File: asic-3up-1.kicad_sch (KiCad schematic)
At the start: 64 parts, among them J14 Conn_01x01, J15 Conn_01x01, J5 Conn_01x01, J7 Conn_01x01, U48 MCP1824T-1202E/OT, U49 MCP1824T-1202E/OT, U50 MCP1824T-1202E/OT, U51 MCP1824T-0802E, U52 MCP1824T-0802E, U53 MCP1824T-0802E, U54 BM1362AC_MODE1, U55 BM1362AC_MODE0, U56 BM1362AC_MODE1

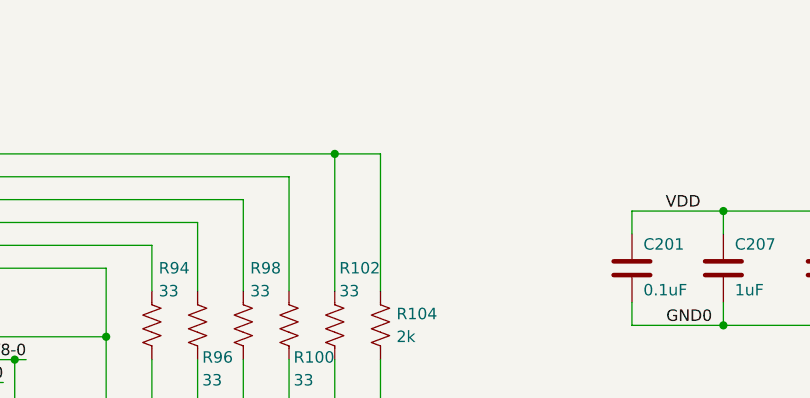
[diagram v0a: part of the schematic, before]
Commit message: added RI pullup resistors for #16. updated BOM. bumped version number to 3
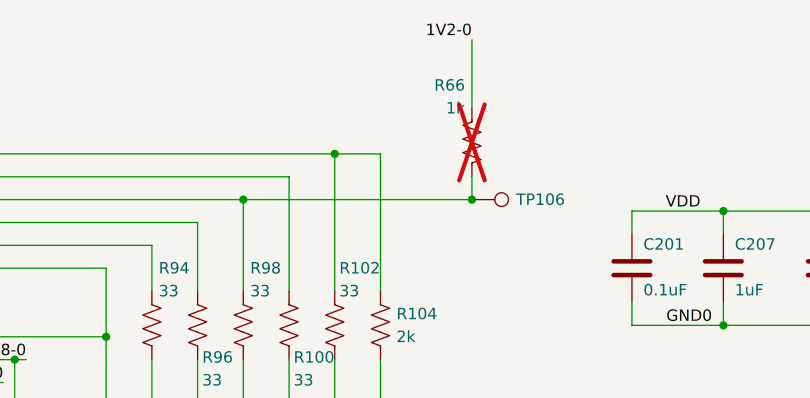
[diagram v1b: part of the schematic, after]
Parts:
- added R66: 1k, Resistor_SMD:R_0402_1005Metric, symbol Device:R_US
- added TP106: TestPoint, TestPoint:TestPoint_Pad_D1.0mm, symbol Connector:TestPoint
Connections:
- net 1V2-0: now also R66.1
- net at R98.1, U54.21 (RI): now also R66.2, TP106.1
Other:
- title: (none) -> emberOne/00
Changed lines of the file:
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@@
 	(paper "A3")
 	(title_block
-		(date "2024-11-25")
-		(rev "2")
+		(title "emberOne/00")
+		(date "2025-02-25")
+		(rev "3")
 	)
 	(text "Reference Voltage Regulators"
@@
 	)
 	(junction
+		(at 328.93 66.04)
+		(diameter 0)
+		(color 0 0 0 0)
+	)
+	(junction
 		(at 64.77 66.04)
 		(diameter 0)
@@
 	)
 	(junction
+		(at 303.53 66.04)
+		(diameter 0)
+		(color 0 0 0 0)
+	)
+	(junction
 		(at 356.87 115.57)
 		(diameter 0)
@@
 	(wire
 		(pts
+			(xy 328.93 48.26) (xy 328.93 55.88)
+		)
+		(stroke
+			(width 0)
+			(type default)
+		)
+	)
+	(wire
+		(pts
 			(xy 224.79 170.18) (xy 231.14 170.18)
 		)
@@
 	(wire
 		(pts
+			(xy 303.53 66.04) (xy 328.93 66.04)
+		)
+		(stroke
+			(width 0)
+			(type default)
+		)
+	)
+	(wire
+		(pts
 			(xy 267.97 132.08) (xy 288.29 132.08)
 		)
@@
 	(wire
 		(pts
+			(xy 328.93 66.04) (xy 328.93 63.5)
+		)
+		(stroke
+			(width 0)
+			(type default)
+		)
+	)
+	(wire
+		(pts
 			(xy 231.14 66.04) (xy 205.74 66.04)
 		)
@@
 		)
 	)
+	(label "1V2-0"
+		(at 328.93 48.26 180)
+		(effects
+			(font
+				(size 1.27 1.27)
+			)
+			(justify right bottom)
+		)
+	)
 	(label "GND1"
 		(at 255.27 160.02 0)
@@
 	)
 	(symbol
+		(lib_id "Connector:TestPoint")
+		(at 328.93 66.04 270)
+		(unit 1)
+		(exclude_from_sim no)
+		(in_bom no)
+		(on_board yes)
+		(dnp no)
+		(property "Reference" "TP106"
+			(at 336.55 66.04 90)
+			(effects
+				(font
+					(size 1.27 1.27)
+				)
+			)
+		)
+		(property "Value" "TestPoint"
+			(at 334.645 67.3099 90)
+			(effects
+				(font
+					(size 1.27 1.27)
+				)
+				(justify left)
+				(hide yes)
+			)
+		)
+		(property "Footprint" "TestPoint:TestPoint_Pad_D1.0mm"
+			(at 328.93 71.12 0)
+			(effects
+				(font
+					(size 1.27 1.27)
+				)
+				(hide yes)
+			)
+		)
+		(property "Datasheet" "~"
+			(at 328.93 71.12 0)
+			(effects
+				(font
+					(size 1.27 1.27)
+				)
+				(hide yes)
+			)
+		)
+		(property "Description" ""
+			(at 328.93 66.04 0)
+			(effects
+				(font
+					(size 1.27 1.27)
+				)
+				(hide yes)
+			)
+		)
+		(pin "1"
+		)
+		(instances
+			(project "emberone"
+				(path "/b036224c-4cdf-48cc-81df-19bc5283ebd2/1041e984-4167-4ef3-8410-dcacf0440a69"
+					(reference "TP106")
+					(unit 1)
+				)
+			)
+		)
+	)
+	(symbol
 		(lib_id "Device:C")
 		(at 152.4 187.96 0)
@@
 					(unit 1)
 				)
+			)
+		)
+	)
+	(symbol
+		(lib_id "Device:R_US")
+		(at 328.93 59.69 0)
+		(mirror y)
+		(unit 1)
+		(exclude_from_sim no)
+		(in_bom yes)
+		(on_board yes)
+		(dnp yes)
+		(property "Reference" "R66"
+			(at 328.168 53.34 0)
+			(effects
+				(font
+					(size 1.27 1.27)
+				)
+				(justify left)
+			)
+		)
+		(property "Value" "1k"
+			(at 328.168 55.88 0)
+			(effects
+				(font
+					(size 1.27 1.27)
+				)
+				(justify left)
+			)
+		)
+		(property "Footprint" "Resistor_SMD:R_0402_1005Metric"
+			(at 327.914 59.944 90)
+			(effects
+				(font
+					(size 1.27 1.27)
+				)
+				(hide yes)
+			)
+		)
+		(property "Datasheet" "~"
+			(at 328.93 59.69 0)
+			(effects
+				(font
+					(size 1.27 1.27)
+				)
+				(hide yes)
+			)
+		)
+		(property "Description" "Resistor, US symbol"
+			(at 328.93 59.69 0)
+			(effects
+				(font
+					(size 1.27 1.27)
+				)
+				(hide yes)
+			)
+		)
+		(property "DK" ""
+			(at 328.93 59.69 0)
+			(effects
+				(font
+					(size 1.27 1.27)
+				)
+				(hide yes)
+			)
+		)
+		(property "PARTNO" ""
+			(at 328.93 59.69 0)
+			(effects
+				(font
+					(size 1.27 1.27)
+				)
+				(hide yes)
+			)
+		)
+		(pin "1"
+		)
+		(pin "2"
+		)
+		(instances
+			(project "emberone"
+				(path "/b036224c-4cdf-48cc-81df-19bc5283ebd2/1041e984-4167-4ef3-8410-dcacf0440a69"
+					(reference "R66")
+					(unit 1)
+				)

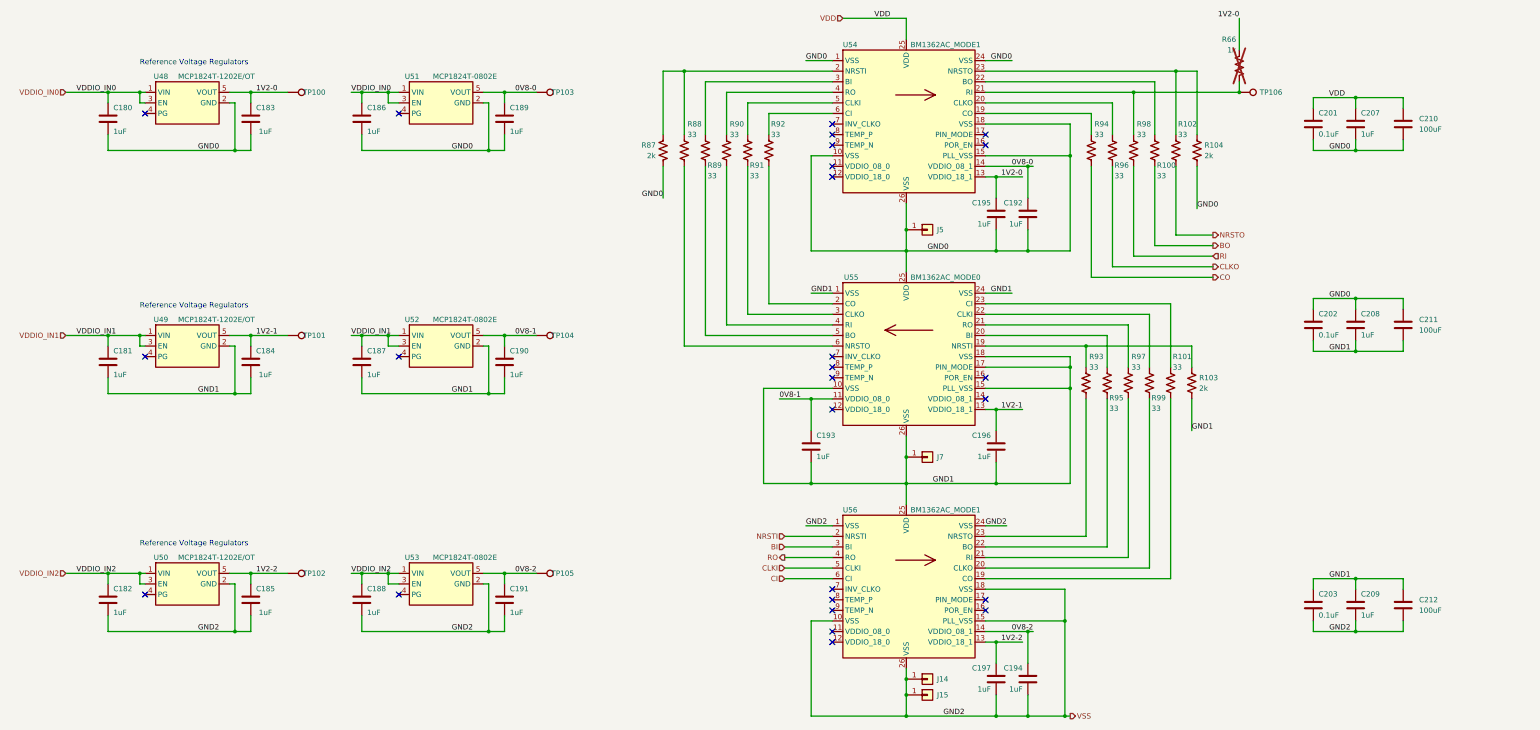
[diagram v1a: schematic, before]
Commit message: added fix for #22. deleted old gerbers
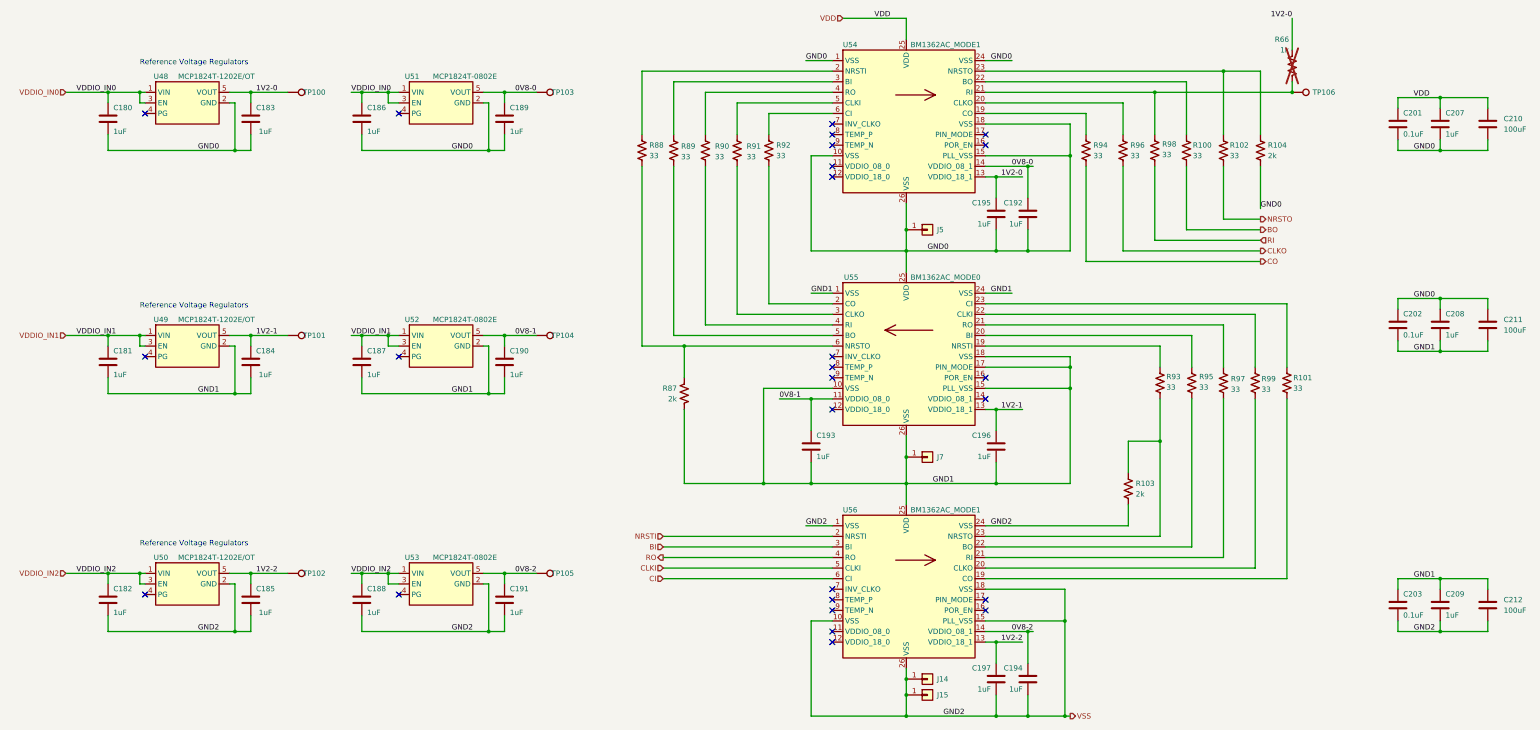
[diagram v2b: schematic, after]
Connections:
- net GND0: no longer R87.2
- net GND1: now also R87.2; no longer R103.2
- net VSS: now also R103.2
- net at R88.1, U54.2 (NRSTI): no longer R87.1
- net at R93.1, U55.19 (NRSTI): no longer R103.1
- net at R88.2, U55.6 (NRSTO): now also R87.1
- net at R93.2, U56.23 (NRSTO): now also R103.1
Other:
- moved on the sheet: C201, C202, C203, C207, C208, C209, C210, C211, C212, R100, R101, R102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

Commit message: DNP low side FET snubber circuit for now (to be redone in v4). Update current sense resistor filter values. regenerate BOM, iBOM. Slight slikscreen cleanup. regenerated gerbers
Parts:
- J14, J15, J5, J7: now left out of the parts list
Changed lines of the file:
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@@
 		(unit 1)
 		(exclude_from_sim no)
-		(in_bom yes)
+		(in_bom no)
 		(on_board yes)
 		(dnp no)
@@
 		(unit 1)
 		(exclude_from_sim no)
-		(in_bom yes)
+		(in_bom no)
 		(on_board yes)
 		(dnp no)
@@
 		(unit 1)
 		(exclude_from_sim no)
-		(in_bom yes)
+		(in_bom no)
 		(on_board yes)
 		(dnp no)
@@
 		(unit 1)
 		(exclude_from_sim no)
-		(in_bom yes)
+		(in_bom no)
 		(on_board yes)
 		(dnp no)

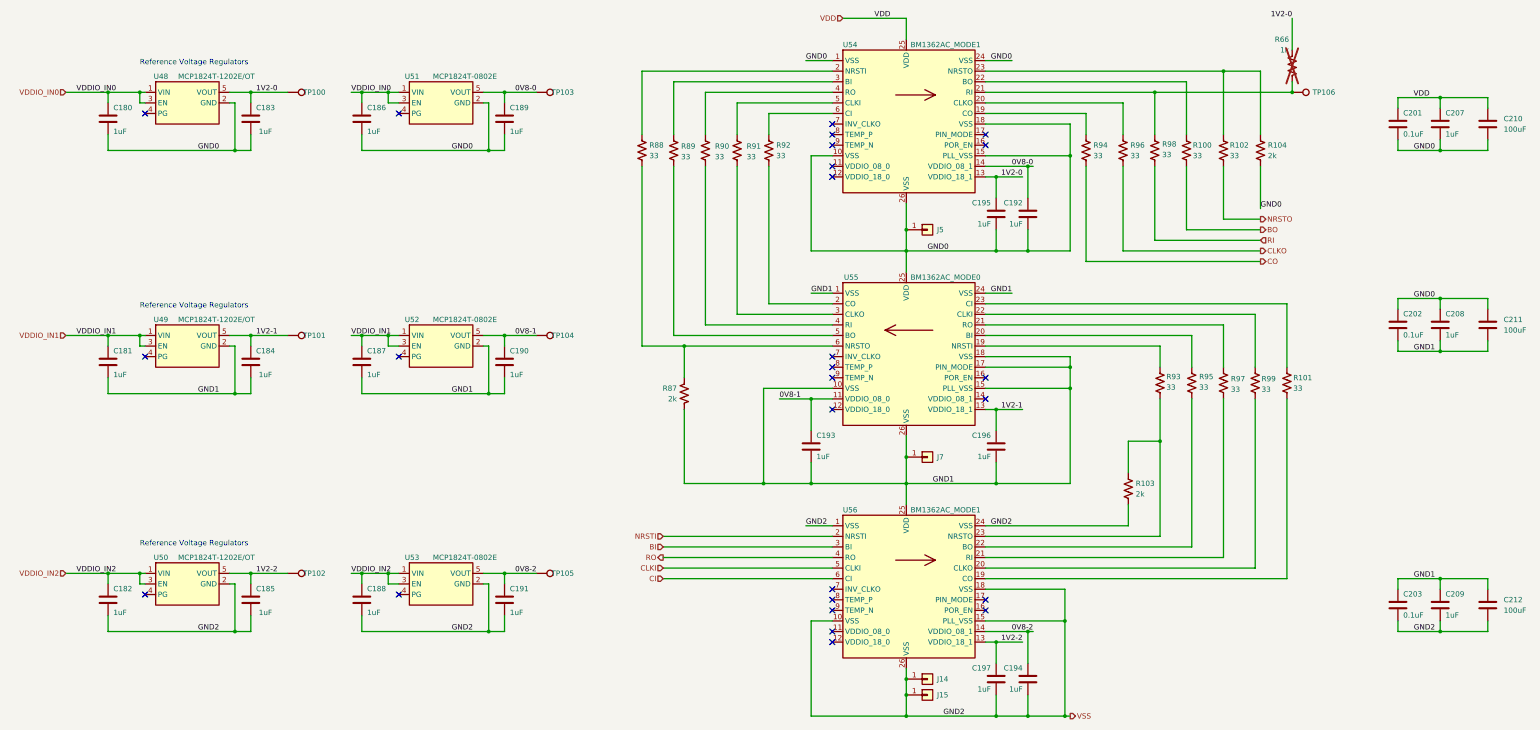
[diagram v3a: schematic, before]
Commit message: Added Mfg to BOM
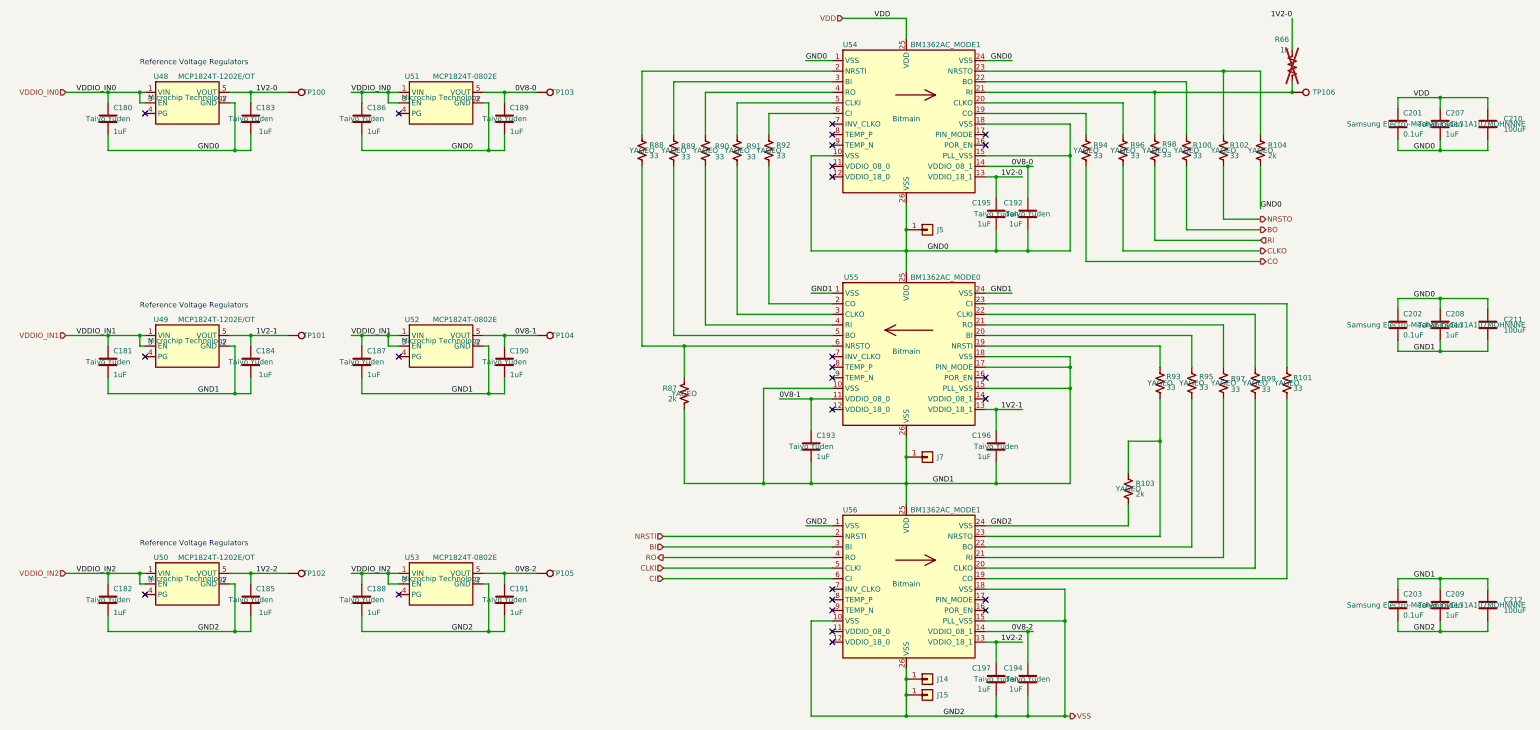
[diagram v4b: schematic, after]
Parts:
- C180, C181, C182, C183, C184, C185, C186, C187, C188, C189, C190, C191, C192, C193, C194, C195, C196, C197, C207, C208, C209: Manufacturer (none) -> Taiyo Yuden
- C201, C202, C203: Manufacturer (none) -> Samsung Electro-Mechanics
- C210, C211, C212: Manufacturer (none) -> CL31A107MQHNNNE
- R100, R101, R102, R103, R104, R87, R88, R89, R90, R91, R92, R93, R94, R95, R96, R97, R98, R99: Manufacturer (none) -> YAGEO
- U48, U49, U50, U51, U52, U53: Manufacturer (none) -> Microchip Technology
- U54, U55, U56: Manufacturer (none) -> Bitmain

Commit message: missed a few
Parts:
- U54, U55, U56: PARTNO (none) -> BM1362AC
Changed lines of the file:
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@@
+			)
+		)
+		(property "PARTNO" "BM1362AC"
+			(at 248.92 72.39 0)
+			(effects
+				(font
+					(size 1.27 1.27)
+				)
 			)
 		)
@@
 			)
 		)
+		(property "PARTNO" "BM1362AC"
+			(at 248.92 128.27 0)
+			(effects
+				(font
+					(size 1.27 1.27)
+				)
+			)
+		)
 		(pin "10"
 		)
@@
 			(at 248.92 184.15 0)
 			(effects
+				(font
+					(size 1.27 1.27)
+				)
+			)
+		)
+		(property "PARTNO" "BM1362AC"
+			(at 248.92 184.15 0)
+			(effects

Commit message: Revert "Merge commit '7c9b4c648e8c0cd5eb9ee29b12963992edc9d4fe' into v4"
This reverts commit 16575a5f433ae2a288f6a827ad209afb5e5f3437, reversing
changes made to e5a5abad8ce065f31a2bf126cd7235584780cb09.
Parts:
- C180, C181, C182, C183, C184, C185, C186, C187, C188, C189, C190, C191, C192, C193, C194, C195, C196, C197, C207, C208, C209: Manufacturer Taiyo Yuden -> (none)
- C201, C202, C203: DK 1276-1234-1-ND -> 478-KGM05AR71C104KHCT-ND; Manufacturer Samsung Electro-Mechanics -> (none); PARTNO CL05A104KO5NNNC -> KGM05AR71C104KH
- C210, C211, C212: Manufacturer CL31A107MQHNNNE -> (none)
- J14, J15, J5, J7: now in the parts list
- R100, R101, R102, R103, R104, R87, R88, R89, R90, R91, R92, R93, R94, R95, R96, R97, R98, R99: Manufacturer YAGEO -> (none)
- R66: now left out of the parts list
- U48, U49, U50: ALT1 (none) -> LDK120M12R; Manufacturer Microchip Technology -> (none)
- U51, U52, U53: ALT1 (none) -> LDK120M08R; Manufacturer Microchip Technology -> (none)
- U54, U55, U56: Manufacturer Bitmain -> (none); PARTNO BM1362AC -> (none)

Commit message: added some LCSC parts numbers and regenerated BOM
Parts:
- C180, C181, C182, C183, C184, C185, C186, C187, C188, C189, C190, C191, C192, C193, C194, C195, C196, C197, C207, C208, C209: LCSC (none) -> C52923
- C201, C202, C203: LCSC (none) -> C307331
- C210, C211, C212: LCSC (none) -> C15008
- R100, R101, R102, R88, R89, R90, R91, R92, R93, R94, R95, R96, R97, R98, R99: LCSC (none) -> C25105
- R103, R104, R87: LCSC (none) -> C60488
